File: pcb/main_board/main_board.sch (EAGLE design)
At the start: 33 parts, among them J1 MEM2067-02-180-00-A_REVB, U1 ADM3101EARQZ-REELRQ_16_ADI-L, U13 SPX3819-3.3

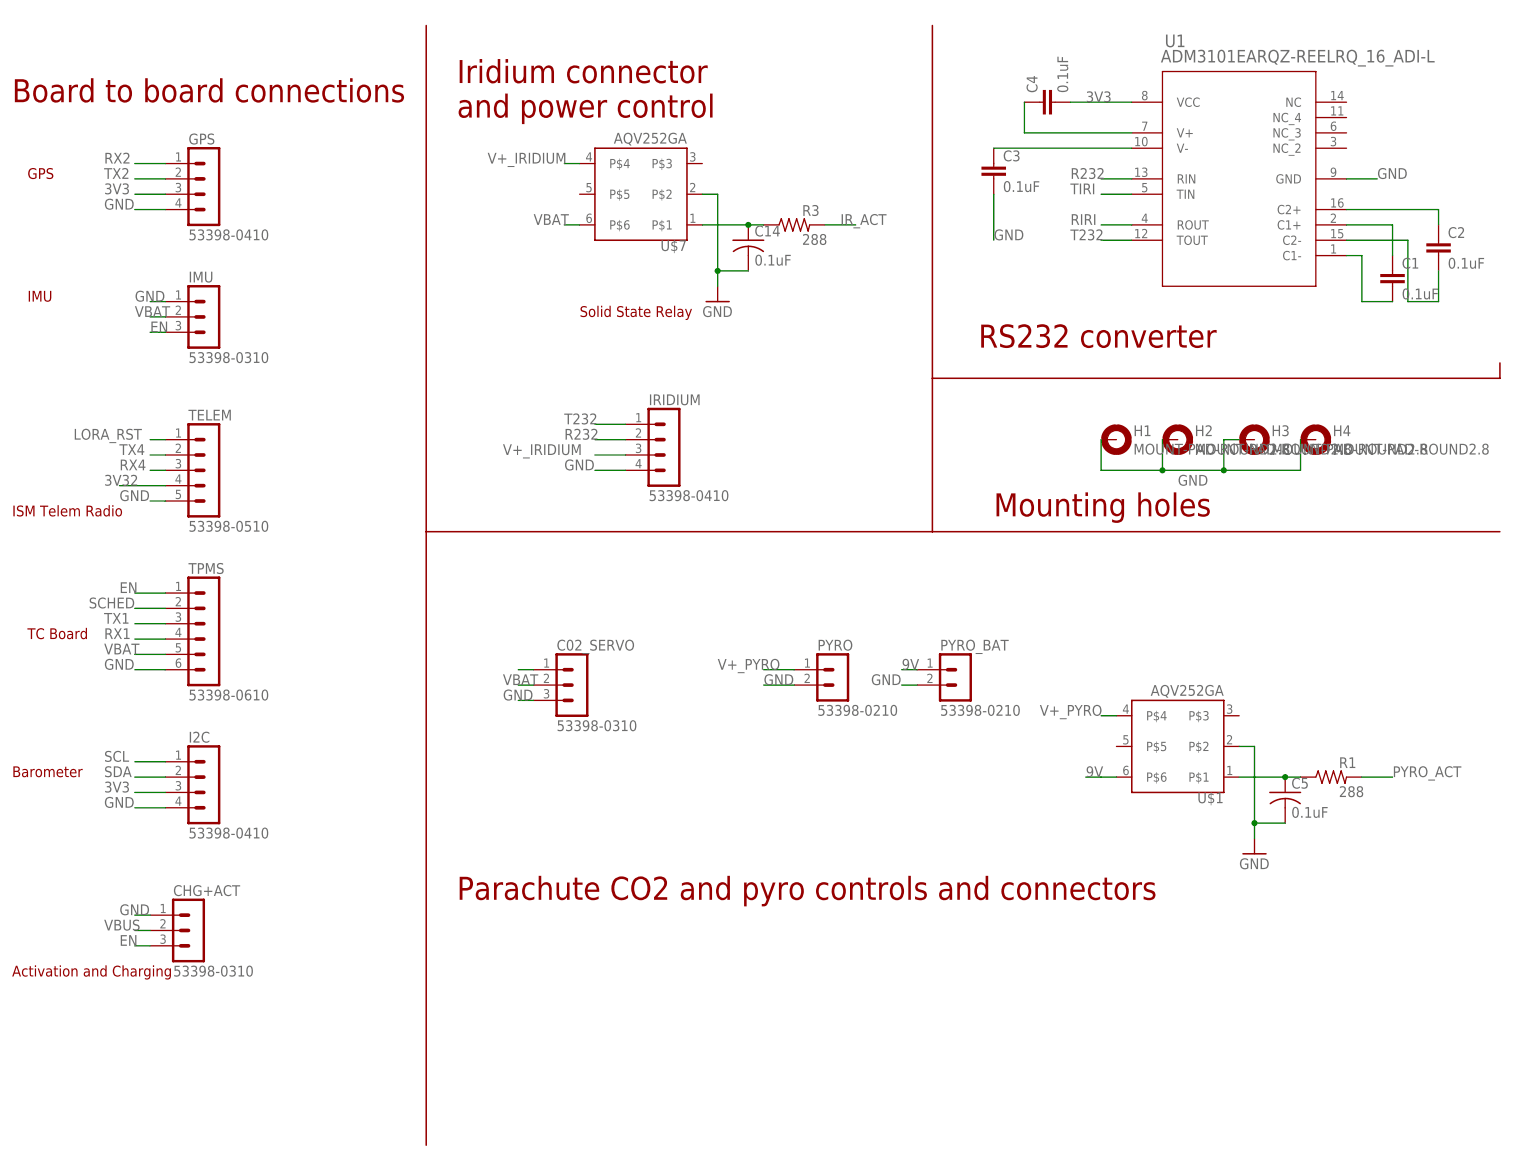
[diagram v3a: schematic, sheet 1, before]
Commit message: updated main board to have new rs232 transceiver and optional mosfets for pyro and iridium power control
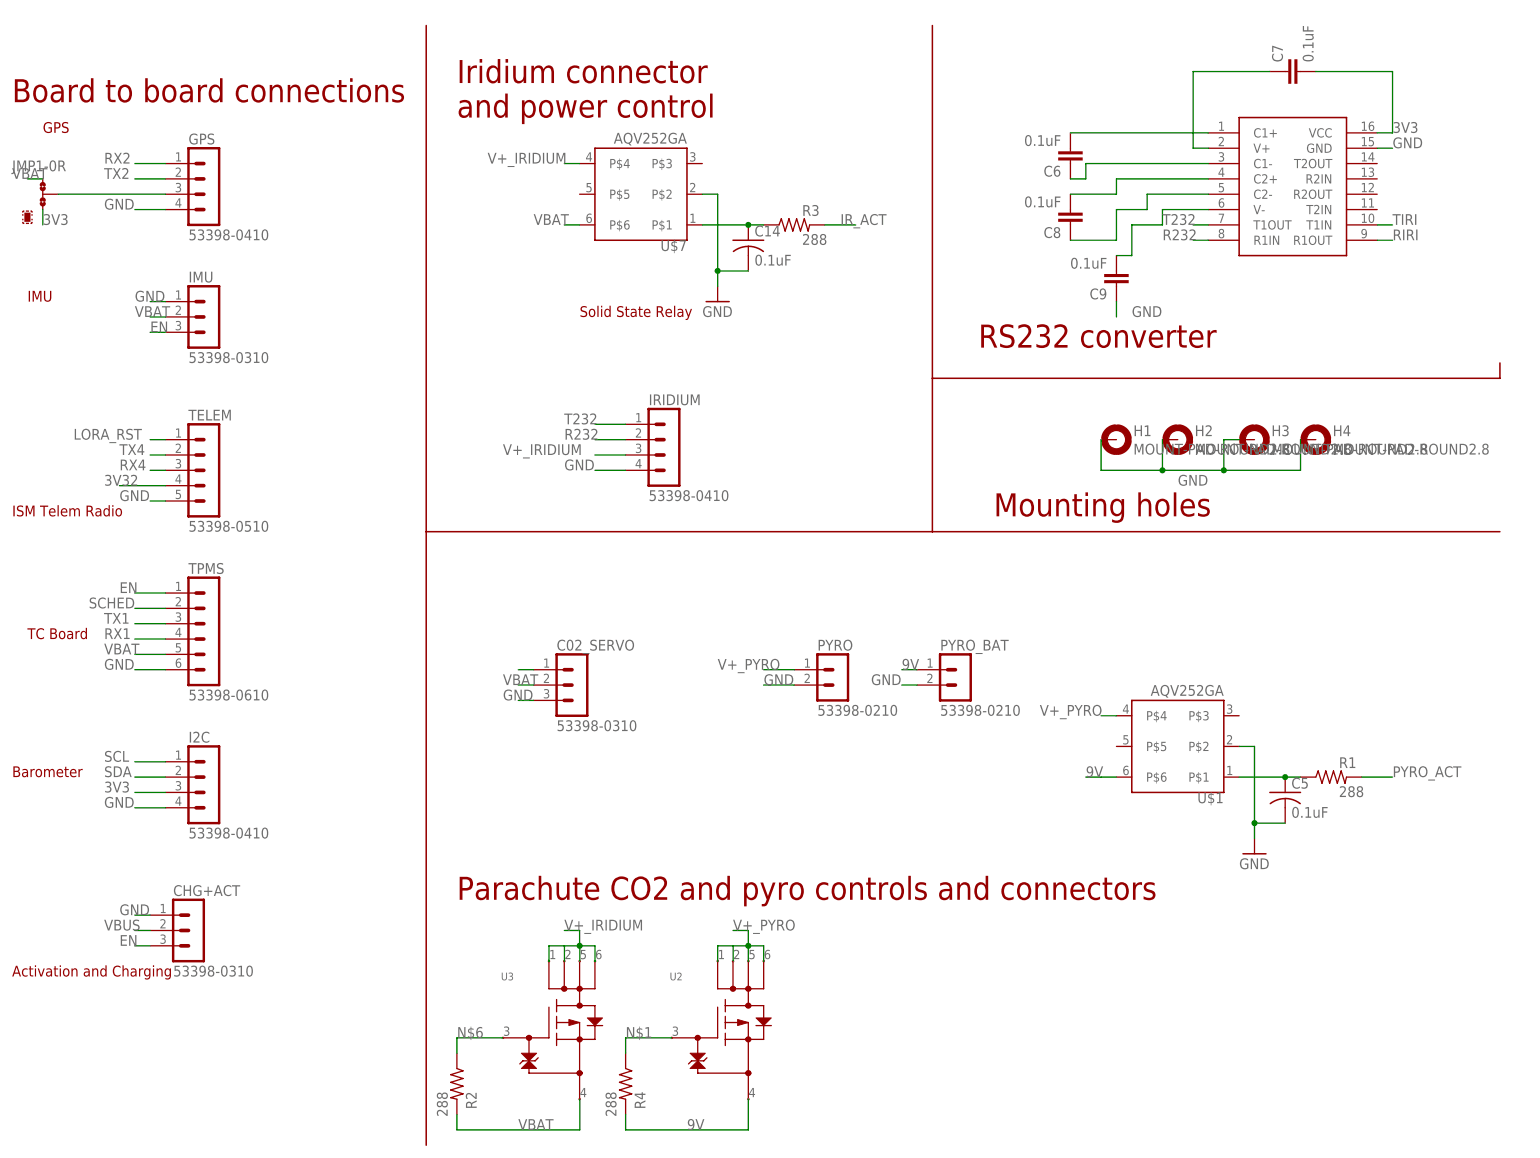
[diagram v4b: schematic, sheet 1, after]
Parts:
- removed C1, C2, C3, C4: 0.1uF, rcl:C-EUC0603
- removed U1: ADM3101EARQZ-REELRQ_16_ADI-L, ADM310:ADM3101EARQZ-REELRQ_16_ADI-L
- added C6, C7, C8, C9: 0.1uF, rcl:C-EUC0603
- added JMP1: 0R-JUMPA, jump-0r-smd:0R-JUMPA
- added R2, R4: 288, adafruit:R-US_R0603
- added U$2: UM3232EEAE, ADM310:UM3232EEAE
- added U2, U3: SSM6J414TU, ssm6j414tu:SSM6J414TU
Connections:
- removed net N$10: C2.2, U1.C2-
- removed net N$3: C4.1, U1.V+
- removed net N$4: C3.1, U1.V-
- removed net N$7: C2.1, U1.C2+
- removed net N$8: C1.1, U1.C1+
- removed net N$9: C1.2, U1.C1-
- new net N$11: C7.1, U$2.V+
- new net N$12: C6.1, U$2.C1-
- new net N$13: C8.2, U$2.C2+
- new net N$14: C8.1, U$2.C2-
- new net N$15: C9.2, U$2.V-
- new net N$2: GPS.3, JMP1-0R.2
- new net N$5: C6.2, U$2.C1+
- net 3V3: now also C7.2, JMP1-0R.3, U$2.VCC; no longer C4.2, GPS.3, U1.VCC
- net 9V: now also R4.2, U2.4
- net GND: now also C9.1, U$2.GND; no longer C3.2, U1.GND
- net N$1: now also R4.1, U2.3
- net N$6: now also R2.1, U3.3
- net R232: now also U$2.R1IN; no longer U1.RIN
- net RIRI: now also U$2.R1OUT; no longer U1.ROUT
- net T232: now also U$2.T1OUT; no longer U1.TOUT
- net TIRI: now also U$2.T1IN; no longer U1.TIN
- net V+_IRIDIUM: now also U3.1, U3.2, U3.5, U3.6
- net V+_PYRO: now also U2.1, U2.2, U2.5, U2.6
- net VBAT: now also JMP1-0R.1, R2.2, U3.4
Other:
- moved on the sheet: J1

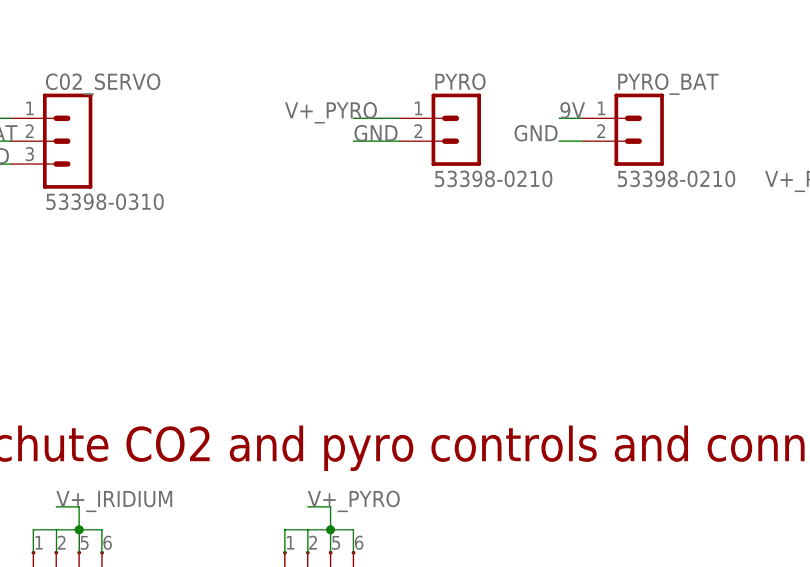
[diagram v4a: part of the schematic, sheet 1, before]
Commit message: updated silkscreen and exported cam files for main board
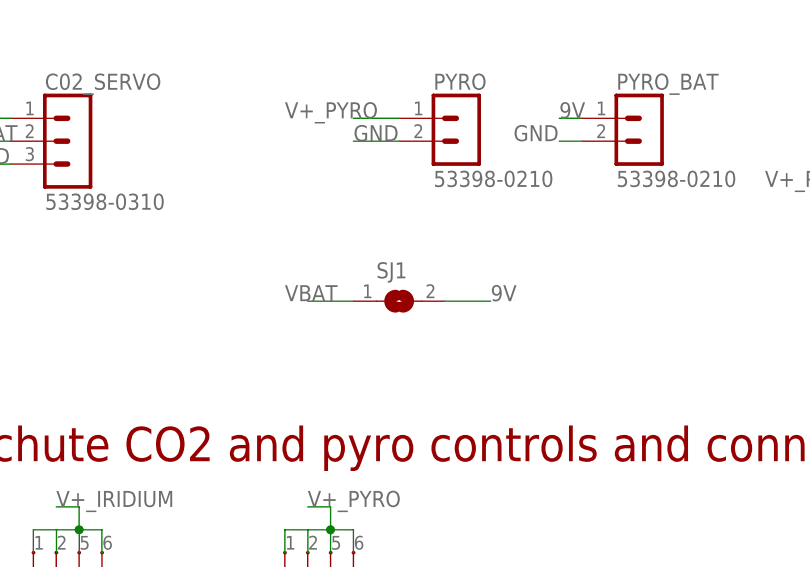
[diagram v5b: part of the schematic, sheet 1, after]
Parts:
- added SJ1: (no value), jumper:SJ
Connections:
- net 9V: now also SJ1.2
- net VBAT: now also SJ1.1
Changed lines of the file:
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@@
 <part name="C8" library="rcl" library_urn="urn:adsk.eagle:library:334" deviceset="C-EU" device="C0603" package3d_urn="urn:adsk.eagle:package:23616/2" value="0.1uF"/>
 <part name="C9" library="rcl" library_urn="urn:adsk.eagle:library:334" deviceset="C-EU" device="C0603" package3d_urn="urn:adsk.eagle:package:23616/2" value="0.1uF"/>
+<part name="SJ1" library="jumper" library_urn="urn:adsk.eagle:library:252" deviceset="SJ" device="" package3d_urn="urn:adsk.eagle:package:15471/1"/>
 </parts>
 <sheets>
@@
 <attribute name="VALUE" x="183.896" y="146.939" size="1.778" layer="96" rot="R180"/>
 </instance>
+<instance part="SJ1" gate="1" x="132.08" y="58.42" smashed="yes">
+<attribute name="NAME" x="129.54" y="60.96" size="1.778" layer="95"/>
+<attribute name="VALUE" x="129.54" y="54.61" size="1.778" layer="96"/>
+</instance>
 </instances>
 <busses>
@@
 <wire x1="7.62" y1="160.02" x2="5.08" y2="160.02" width="0.1524" layer="91"/>
 <label x="2.54" y="160.02" size="1.778" layer="95"/>
+</segment>
+<segment>
+<pinref part="SJ1" gate="1" pin="1"/>
+<wire x1="127" y1="58.42" x2="121.92" y2="58.42" width="0.1524" layer="91"/>
+<label x="119.38" y="58.42" size="1.778" layer="95"/>
 </segment>
 </net>
@@
 <label x="114.3" y="2.54" size="1.778" layer="95"/>
 </segment>
-</net>
+<segment>
+<pinref part="SJ1" gate="1" pin="2"/>
+<wire x1="137.16" y1="58.42" x2="142.24" y2="58.42" width="0.1524" layer="91"/>
+<label x="142.24" y="58.42" size="1.778" layer="95"/>
+</segment>
+</net>
